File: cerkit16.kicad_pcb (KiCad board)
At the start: 2 copper layers, 35 parts, among them U1 ProMicro

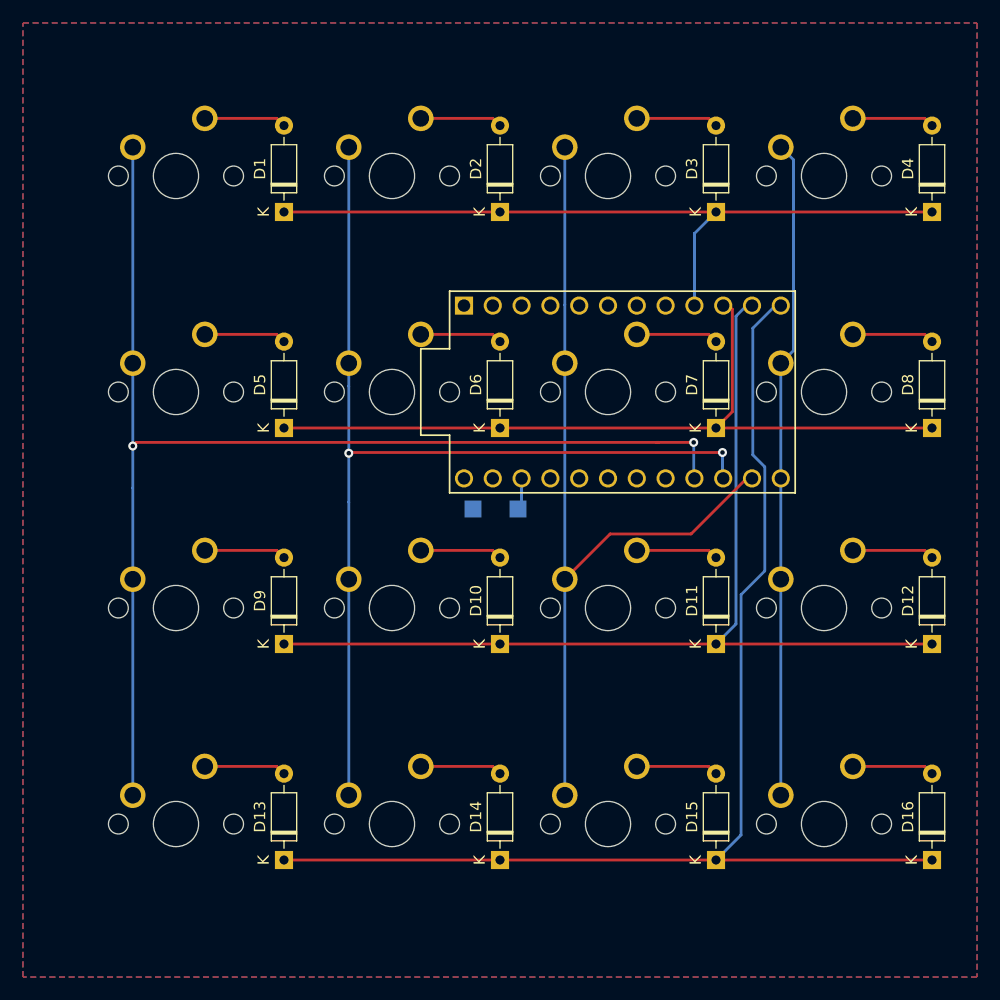
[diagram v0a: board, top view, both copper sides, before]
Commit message: Added edge cuts with curved corners
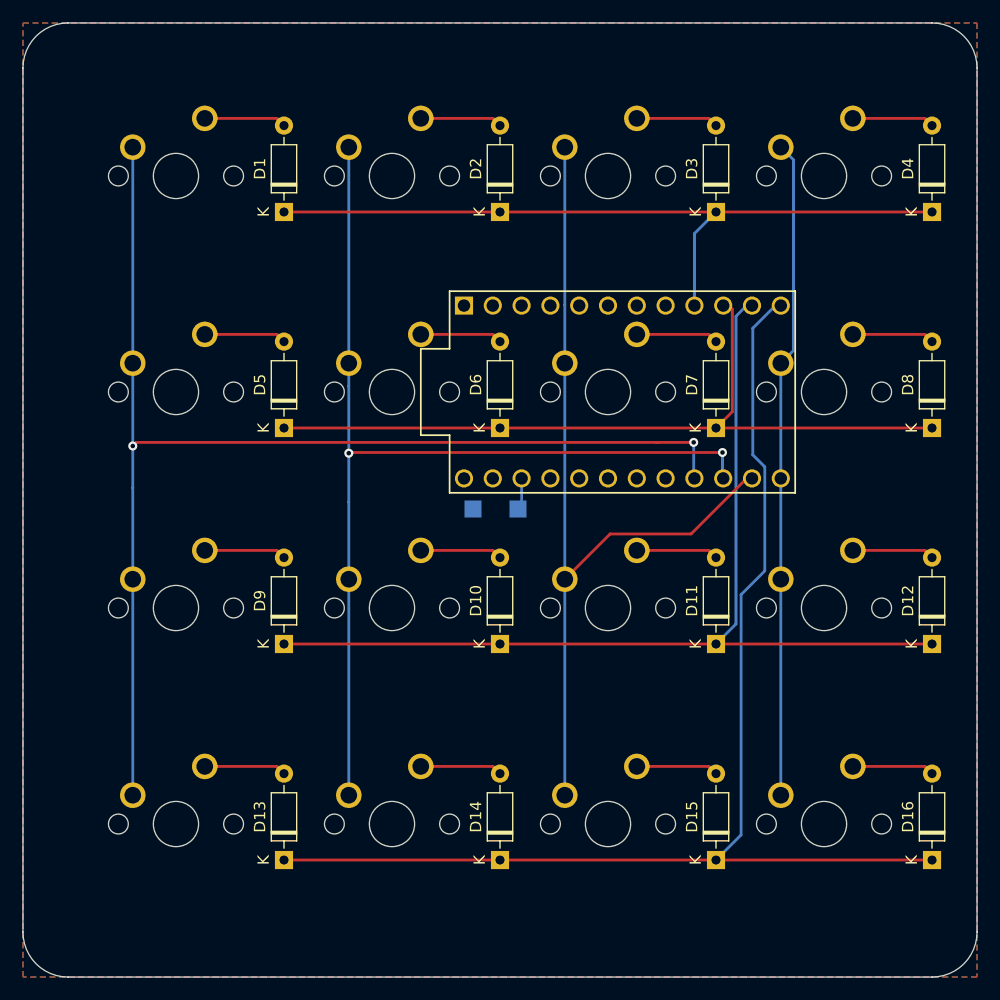
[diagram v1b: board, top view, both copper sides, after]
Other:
- board outline added: 84.1 x 84.1 mm

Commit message: reduced the board size
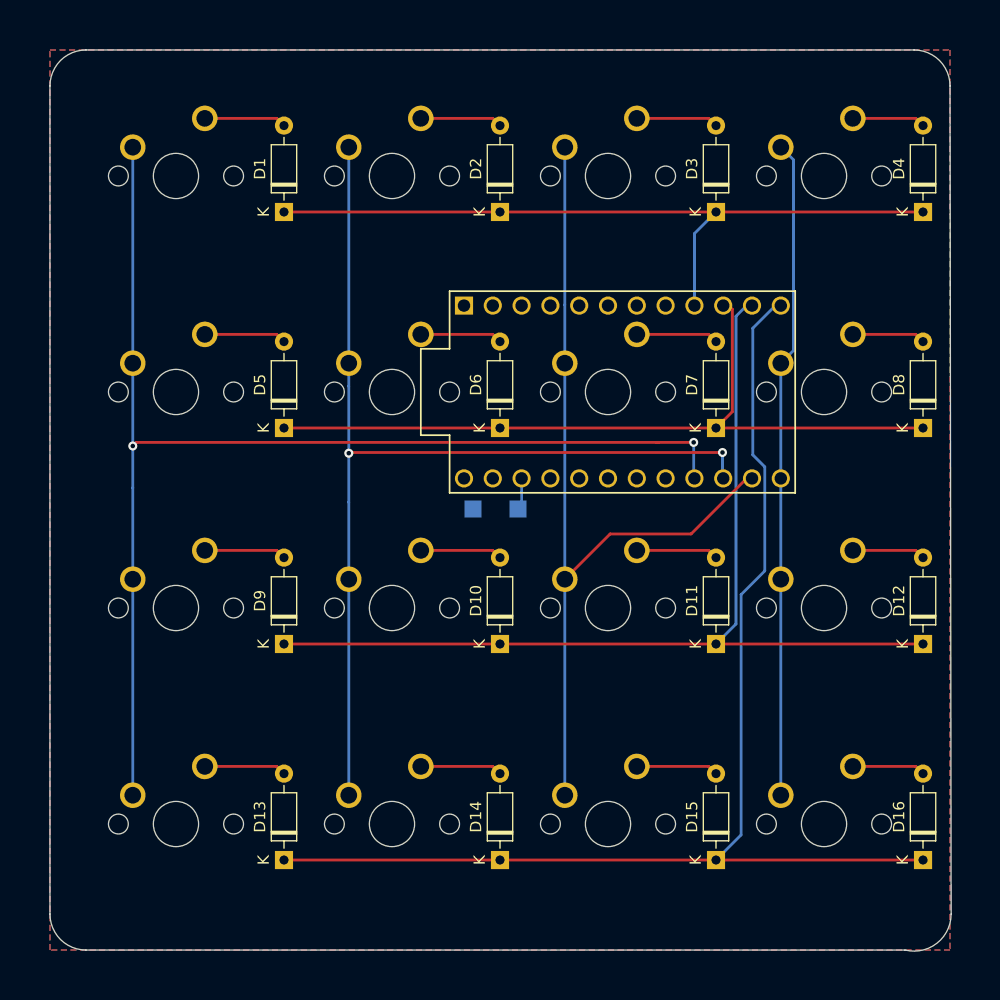
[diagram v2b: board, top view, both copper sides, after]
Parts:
- moved D12 0.79 mm to (115.1, 82.5)
- moved D16 0.79 mm to (115.1, 101.6)
- moved D4 0.79 mm to (115.1, 44.5)
- moved D8 0.79 mm to (115.1, 63.5)
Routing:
- net ROW2: track 88.8 -> 88.0 mm
- net ROW3: track 109.8 -> 109.0 mm
- net ROW1: track 69.3 -> 68.6 mm
- net ROW0: track 65.7 -> 64.9 mm
- net Net-(D8-Pad2): track 7.25 -> 6.45 mm
- net Net-(D4-Pad2): track 7.25 -> 6.45 mm
- net Net-(D16-Pad2): track 7.25 -> 6.45 mm
- net Net-(D12-Pad2): track 7.25 -> 6.45 mm
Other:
- board size 84.1 x 84.1 mm -> 79.5 x 79.5 mm

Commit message: added gerbers
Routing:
- removed copper zone on B.Cu, net GND
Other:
- board size 79.5 x 79.5 mm -> 76.2 x 76.2 mm
